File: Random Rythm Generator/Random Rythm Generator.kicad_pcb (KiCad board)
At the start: 2 copper layers, 72.4 x 58.2 mm, 28 parts, among them SW1 SW_Push, U1 LM78L05_TO92, U2 40106, U3 4040, U4 74LS165

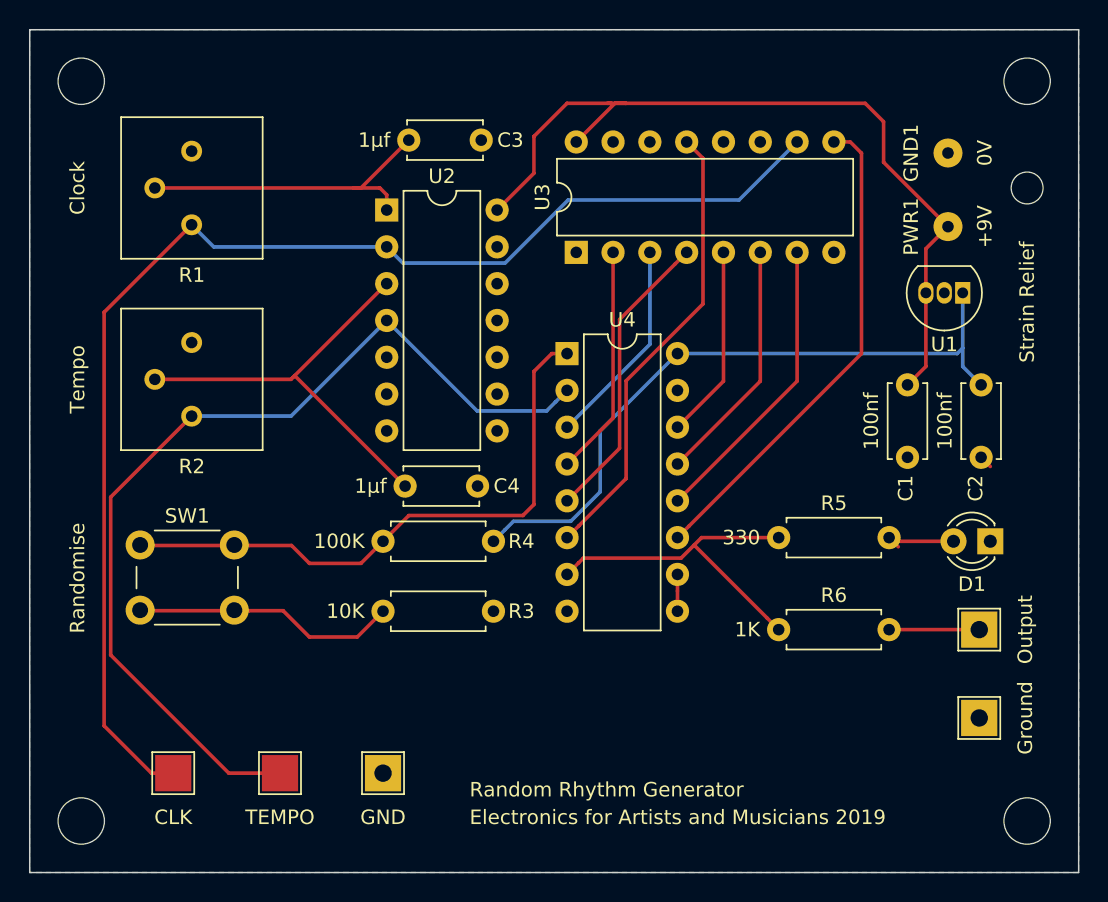
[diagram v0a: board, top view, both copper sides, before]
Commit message: add smoothing capacitor to power supply
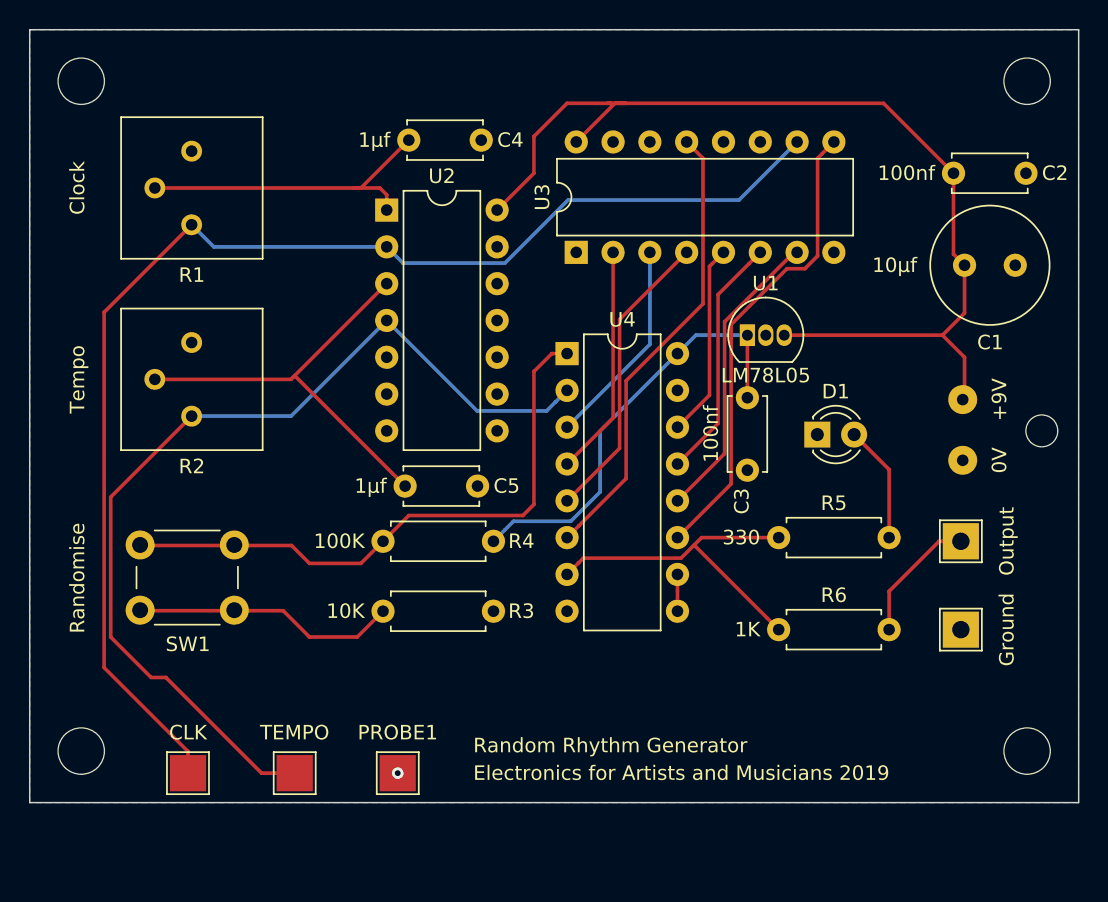
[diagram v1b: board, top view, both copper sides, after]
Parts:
- added C3: 100nf, Capacitor_THT:C_Disc_D5.0mm_W2.5mm_P5.00mm, F.Cu at (134.4, 71.6)
- C1: value 100nf -> 10µf; footprint Capacitor_THT:C_Disc_D5.0mm_W2.5mm_P5.00mm -> Capacitor_THT:C_Radial_D8.0mm_H7.0mm_P3.50mm
- PROBE1: footprint TestPoint:TestPoint_THTPad_2.5x2.5mm_Drill1.2mm -> TestPoint:TestPoint_Pad_2.5x2.5mm
- U1: value LM78L05_TO92 -> LM78L05
- moved GND1 21.2 mm to (149.2, 75.9)
- moved REF** 16.8 mm to (154.7, 73.9)
- moved U1 15.1 mm to (134.4, 67.3), turned to 0 degrees
- moved C2 14.7 mm to (148.6, 56.1), turned to 0 degrees
- moved D1 14.0 mm to (139.2, 74.2), turned to 0 degrees
- moved PWR1 12.0 mm to (149.2, 71.8)
- moved C1 9.15 mm to (149.4, 62.5), turned to 0 degrees
- moved Output2 6.23 mm to (149.1, 87.6)
- moved Output1 6.23 mm to (149.1, 81.5)
- moved REF** 4.83 mm to (88.4, 96.0)
- moved REF** 4.83 mm to (153.7, 96.0)
- moved PROBE1 1.02 mm to (110.2, 97.5)
- moved PROBE2 1.02 mm to (95.8, 97.5)
- moved PROBE3 1.02 mm to (103.1, 97.5)
- renumbered C3 to C4, C4 to C5
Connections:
- C2 pad 1: +5V -> +9V
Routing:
- net +5V: track 47.3 -> 30.2 mm
- net +9V: track 57.9 -> 71.0 mm
- net Net-(Output1-Pad1): track 6.22 -> 9.39 mm
- net Net-(D1-Pad2): track 5.45 -> 8.47 mm
- net Net-(U3-Pad9): track 34.0 -> 32.5 mm
- net GND: track 0.90 -> 0.00 mm, vias 0 -> 1
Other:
- board size 72.4 x 58.2 mm -> 72.4 x 53.3 mm

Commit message: neaten schematic and pcb layout slightly
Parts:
- SW1: value SW_Push -> Randomise
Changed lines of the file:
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@@
   (layers
     (0 F.Cu signal)
-    (31 B.Cu signal hide)
+    (31 B.Cu signal)
     (33 F.Adhes user)
     (35 F.Paste user)
@@
       (effects (font (size 1 1) (thickness 0.15)))
     )
-    (fp_text value SW_Push (at 3.302 -2.286) (layer F.Fab)
+    (fp_text value Randomise (at 3.302 -2.286) (layer F.Fab)
       (effects (font (size 1 1) (thickness 0.15)))
     )
@@
   (gr_line (start 157.226 99.568) (end 84.836 99.568) (layer Edge.Cuts) (width 0.1))
   (gr_line (start 157.226 46.228) (end 157.226 99.568) (layer Edge.Cuts) (width 0.1))
-  (gr_text "Electronics for Artists and Musicians 2019" (at 115.443 97.536) (layer F.SilkS)
+  (gr_text "Electronics for Artists and Musicians 2019" (at 115.443 98.552) (layer F.SilkS)
     (effects (font (size 1 1) (thickness 0.15)) (justify left))
   )
-  (gr_text "Random Rhythm Generator" (at 115.443 95.631) (layer F.SilkS)
+  (gr_text "Random Rhythm Generator" (at 115.443 96.647) (layer F.SilkS)
     (effects (font (size 1 1) (thickness 0.15)) (justify left))
   )
@@
   (segment (start 107.696 57.15) (end 107.188 57.15) (width 0.25) (layer F.Cu) (net 4))
   (segment (start 93.472 57.15) (end 107.188 57.15) (width 0.25) (layer F.Cu) (net 4))
-  (segment (start 93.472 70.358) (end 102.87 70.358) (width 0.25) (layer F.Cu) (net 21))
-  (segment (start 102.87 70.358) (end 102.997 70.231) (width 0.25) (layer F.Cu) (net 21))
-  (segment (start 110.744 77.724) (end 103.124 70.104) (width 0.25) (layer F.Cu) (net 21))
-  (segment (start 103.124 70.104) (end 109.474 63.754) (width 0.25) (layer F.Cu) (net 21))
-  (segment (start 102.997 70.231) (end 103.124 70.104) (width 0.25) (layer F.Cu) (net 21))
   (segment (start 144.399 81.534) (end 144.145 81.28) (width 0.25) (layer F.Cu) (net 5))
   (segment (start 144.145 76.581) (end 144.145 81.28) (width 0.25) (layer F.Cu) (net 5))
@@
   (segment (start 136.525 87.63) (end 135.725001 86.830001) (width 0.25) (layer F.Cu) (net 20))
   (segment (start 131.205002 81.28) (end 130.690001 81.795001) (width 0.25) (layer F.Cu) (net 20))
+  (segment (start 93.472 70.358) (end 102.87 70.358) (width 0.25) (layer F.Cu) (net 21))
+  (segment (start 102.87 70.358) (end 102.997 70.231) (width 0.25) (layer F.Cu) (net 21))
+  (segment (start 110.744 77.724) (end 103.124 70.104) (width 0.25) (layer F.Cu) (net 21))
+  (segment (start 103.124 70.104) (end 109.474 63.754) (width 0.25) (layer F.Cu) (net 21))
+  (segment (start 102.997 70.231) (end 103.124 70.104) (width 0.25) (layer F.Cu) (net 21))
   (zone (net 1) (net_name GND) (layer B.Cu) (hatch edge 0.508)
     (connect_pads (clearance 0.508))

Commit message: minor PCB and schematic tweaks
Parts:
- C2: value 100nf -> 330nf
- U1: value LM78L05 -> LM78L05_TO92
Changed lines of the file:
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@@
       (effects (font (size 1 1) (thickness 0.15)) (justify left))
     )
-    (fp_text value 100nf (at -1.27 0) (layer F.SilkS)
+    (fp_text value 330nf (at -1.27 0) (layer F.SilkS)
       (effects (font (size 1 1) (thickness 0.15)) (justify right))
     )
@@
       (effects (font (size 1 1) (thickness 0.15)))
     )
-    (fp_text value LM78L05 (at 1.27 2.79) (layer F.SilkS)
-      (effects (font (size 1 1) (thickness 0.15)))
-    )
+    (fp_text value LM78L05_TO92 (at 1.27 2.79) (layer F.SilkS)
+      (effects (font (size 1 1) (thickness 0.15)))
+    )

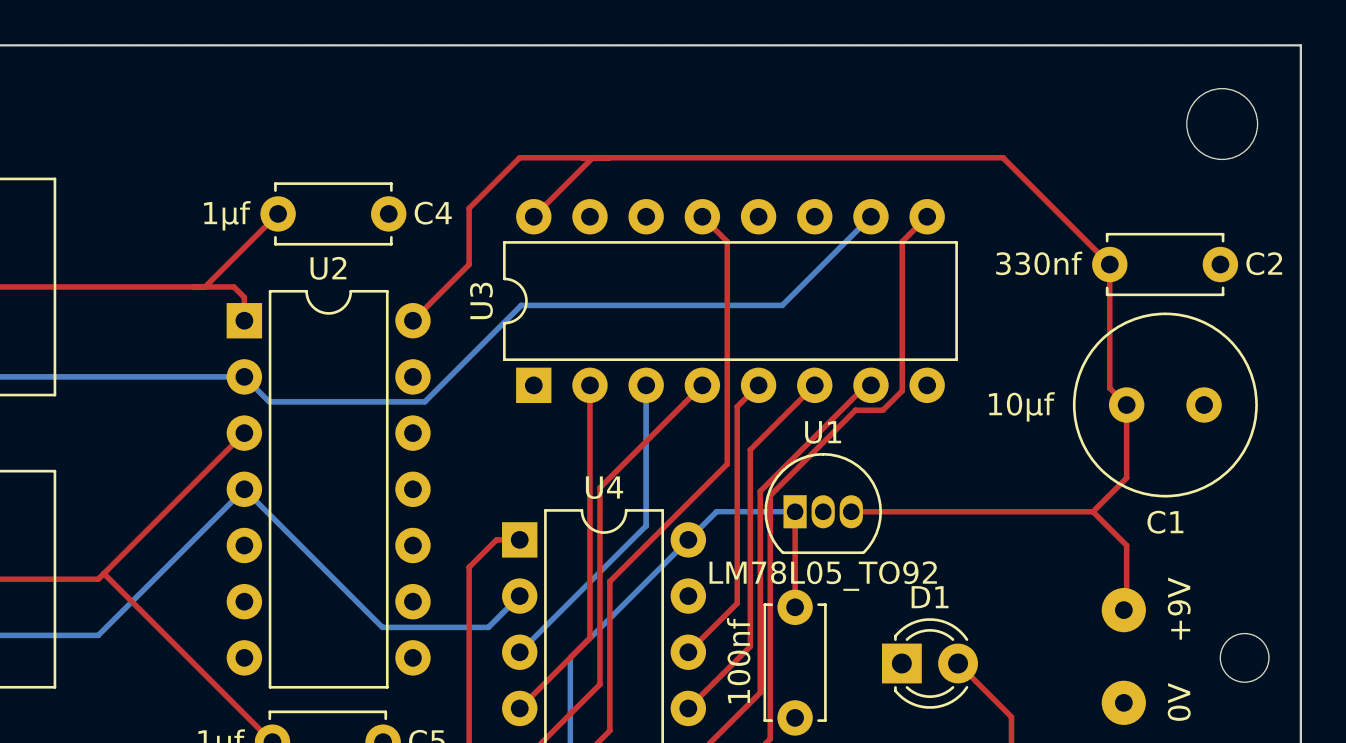
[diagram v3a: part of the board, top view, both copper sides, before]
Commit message: move decoupling capacitors closer to ICs
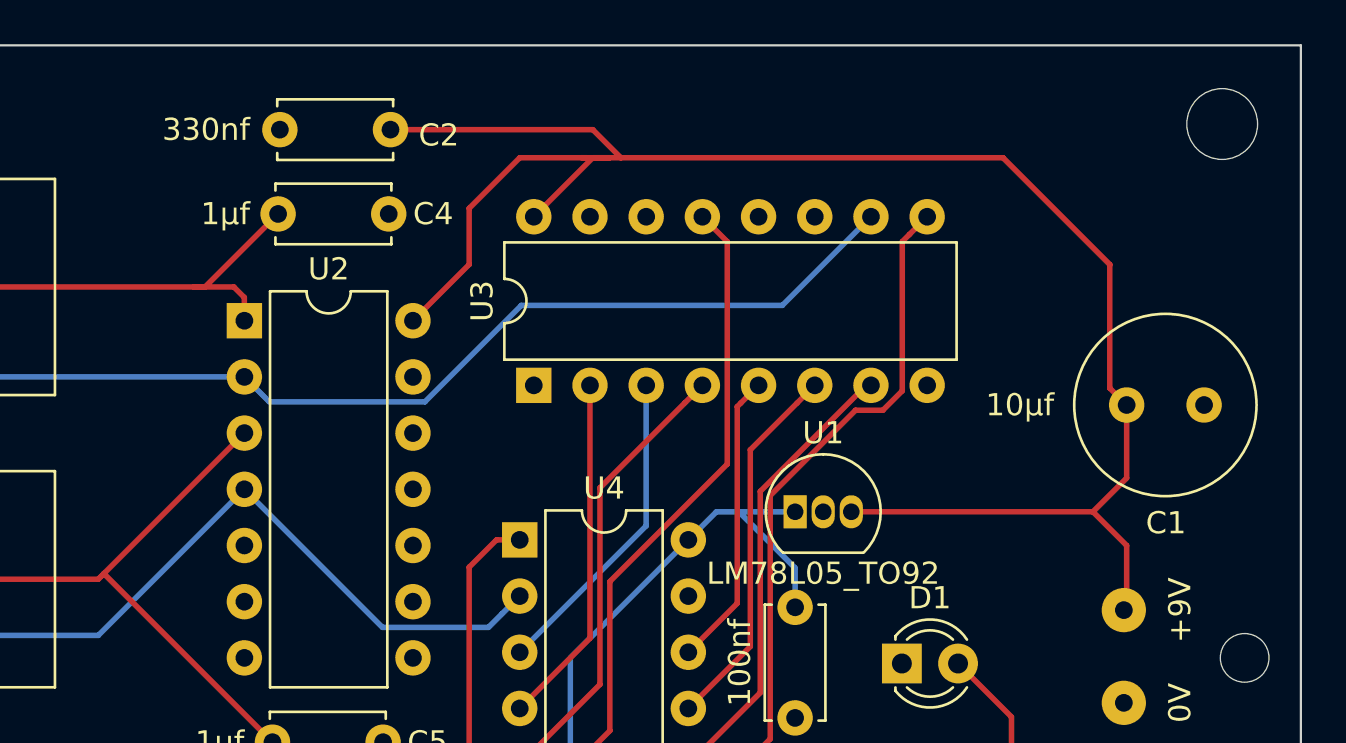
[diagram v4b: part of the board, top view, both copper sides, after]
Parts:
- moved C2 33.1 mm to (116.1, 50.0), turned to 180 degrees
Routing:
- net +9V: track 71.0 -> 81.9 mm
- net +5V: track 30.2 -> 31.3 mm
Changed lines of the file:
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@@
     (thickness 1.6)
     (drawings 6)
-    (tracks 130)
+    (tracks 135)
     (zones 0)
     (modules 29)
@@
   )
   (module Capacitor_THT:C_Disc_D5.0mm_W2.5mm_P5.00mm (layer F.Cu)
-    (at 148.59 56.134)
+    (at 116.078 50.038 180)
     (descr "C, Disc series, Radial, pin pitch=5.00mm, , diameter*width=5*2.5mm^2, Capacitor, http://cdn-reichelt.de/documents/datenblatt/B300/DS_KERKO_TC.pdf")
     (tags "C Disc series Radial pin pitch 5.00mm  diameter 5mm width 2.5mm Capacitor")
-    (fp_text reference C2 (at 6.096 0) (layer F.SilkS)
+    (fp_text reference C2 (at -1.27 -0.254) (layer F.SilkS)
       (effects (font (size 1 1) (thickness 0.15)) (justify left))
     )
-    (fp_text value 330nf (at -1.27 0) (layer F.SilkS)
+    (fp_text value 330nf (at 6.35 0) (layer F.SilkS)
       (effects (font (size 1 1) (thickness 0.15)) (justify right))
     )
@@
     (fp_line (start 0 1.25) (end 5 1.25) (layer F.Fab) (width 0.1))
     (fp_line (start 0 -1.25) (end 0 1.25) (layer F.Fab) (width 0.1))
-    (pad 2 thru_hole circle (at 5 0) (size 1.6 1.6) (drill 0.8) (layers *.Cu *.Mask)
-      (net 1 GND))
-    (pad 1 thru_hole circle (at 0 0) (size 1.6 1.6) (drill 0.8) (layers *.Cu *.Mask)
+    (pad 2 thru_hole circle (at 5 0 180) (size 1.6 1.6) (drill 0.8) (layers *.Cu *.Mask)
+      (net 1 GND))
+    (pad 1 thru_hole circle (at 0 0 180) (size 1.6 1.6) (drill 0.8) (layers *.Cu *.Mask)
       (net 2 +9V))
     (model ${KISYS3DMOD}/Capacitor_THT.3dshapes/C_Disc_D5.0mm_W2.5mm_P5.00mm.wrl
@@
   (segment (start 149.352 71.628) (end 149.225 71.755) (width 0.25) (layer F.Cu) (net 2))
   (segment (start 143.764 51.308) (end 148.59 56.134) (width 0.25) (layer F.Cu) (net 2))
-  (segment (start 125.984 51.308) (end 143.764 51.308) (width 0.25) (layer F.Cu) (net 2))
   (segment (start 147.828 67.31) (end 136.906 67.31) (width 0.25) (layer F.Cu) (net 2))
   (segment (start 149.352 68.834) (end 147.828 67.31) (width 0.25) (layer F.Cu) (net 2))
@@
   (segment (start 148.59 61.722) (end 149.352 62.484) (width 0.25) (layer F.Cu) (net 2))
   (segment (start 148.59 56.134) (end 148.59 61.722) (width 0.25) (layer F.Cu) (net 2))
+  (segment (start 116.078 50.038) (end 125.222 50.038) (width 0.25) (layer F.Cu) (net 2))
+  (segment (start 125.222 50.038) (end 126.492 51.308) (width 0.25) (layer F.Cu) (net 2))
+  (segment (start 126.492 51.308) (end 143.764 51.308) (width 0.25) (layer F.Cu) (net 2))
+  (segment (start 125.984 51.308) (end 126.492 51.308) (width 0.25) (layer F.Cu) (net 2))
   (segment (start 117.639999 80.734001) (end 116.84 81.534) (width 0.25) (layer B.Cu) (net 3))
   (segment (start 124.206 78.122999) (end 122.174 80.154999) (width 0.25) (layer B.Cu) (net 3))
@@
   (segment (start 124.206 73.914) (end 124.206 78.122999) (width 0.25) (layer B.Cu) (net 3))
   (segment (start 129.54 68.58) (end 124.206 73.914) (width 0.25) (layer B.Cu) (net 3))
-  (segment (start 134.366 71.628) (end 134.366 67.31) (width 0.25) (layer F.Cu) (net 3))
   (segment (start 130.81 67.31) (end 129.54 68.58) (width 0.25) (layer B.Cu) (net 3))
-  (segment (start 134.366 67.31) (end 130.81 67.31) (width 0.25) (layer B.Cu) (net 3))
+  (segment (start 134.366 69.85) (end 131.826 67.31) (width 0.25) (layer B.Cu) (net 3))
+  (segment (start 131.826 67.31) (end 130.81 67.31) (width 0.25) (layer B.Cu) (net 3))
+  (segment (start 134.366 71.628) (end 134.366 69.85) (width 0.25) (layer B.Cu) (net 3))
+  (segment (start 134.366 67.31) (end 131.826 67.31) (width 0.25) (layer B.Cu) (net 3))
   (segment (start 109.474 57.624) (end 109.474 58.674) (width 0.25) (layer F.Cu) (net 4))
   (segment (start 109 57.15) (end 109.474 57.624) (width 0.25) (layer F.Cu) (net 4))
